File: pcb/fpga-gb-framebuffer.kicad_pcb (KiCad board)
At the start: 2 copper layers, 74.9 x 45.7 mm, 20 parts

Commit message: Updated PCB design
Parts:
- moved GB_LCD1 3.81 mm to (100.3, 69.8)
- moved R1 3.81 mm to (108.0, 72.4)
- moved R2 3.81 mm to (115.6, 69.8)
- moved R3 3.81 mm to (108.0, 77.5)
- moved R4 3.81 mm to (115.6, 74.9)
- moved R6 2.54 mm to (115.6, 82.6)
- moved R7 2.54 mm to (108.0, 92.7)
- moved R5 2.54 mm to (108.0, 85.1)
- moved R8 2.54 mm to (115.6, 90.2)
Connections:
- TinyFPGA_BX1 pad 10: IN_DATA_1 -> Net-(TinyFPGA_BX1-Pad10)
- TinyFPGA_BX1 pad 11: Net-(TinyFPGA_BX1-Pad11) -> IN_PIXEL_CLK
- TinyFPGA_BX1 pad 12: IN_PIXEL_CLK -> Net-(TinyFPGA_BX1-Pad12)
- TinyFPGA_BX1 pad 6: Net-(TinyFPGA_BX1-Pad6) -> IN_DATA_0
- TinyFPGA_BX1 pad 8: Net-(TinyFPGA_BX1-Pad8) -> IN_DATA_1
- TinyFPGA_BX1 pad 9: IN_DATA_0 -> Net-(TinyFPGA_BX1-Pad9)
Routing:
- net GB_GND: track 153.8 -> 0.00 mm
- net GB_PIXEL_CLK: track 10.8 -> 13.3 mm
- net GB_VSYNC: track 11.3 -> 13.3 mm
- net IN_DATA_0: track 8.01 -> 6.44 mm
- net IN_DATA_1: track 6.96 -> 6.44 mm

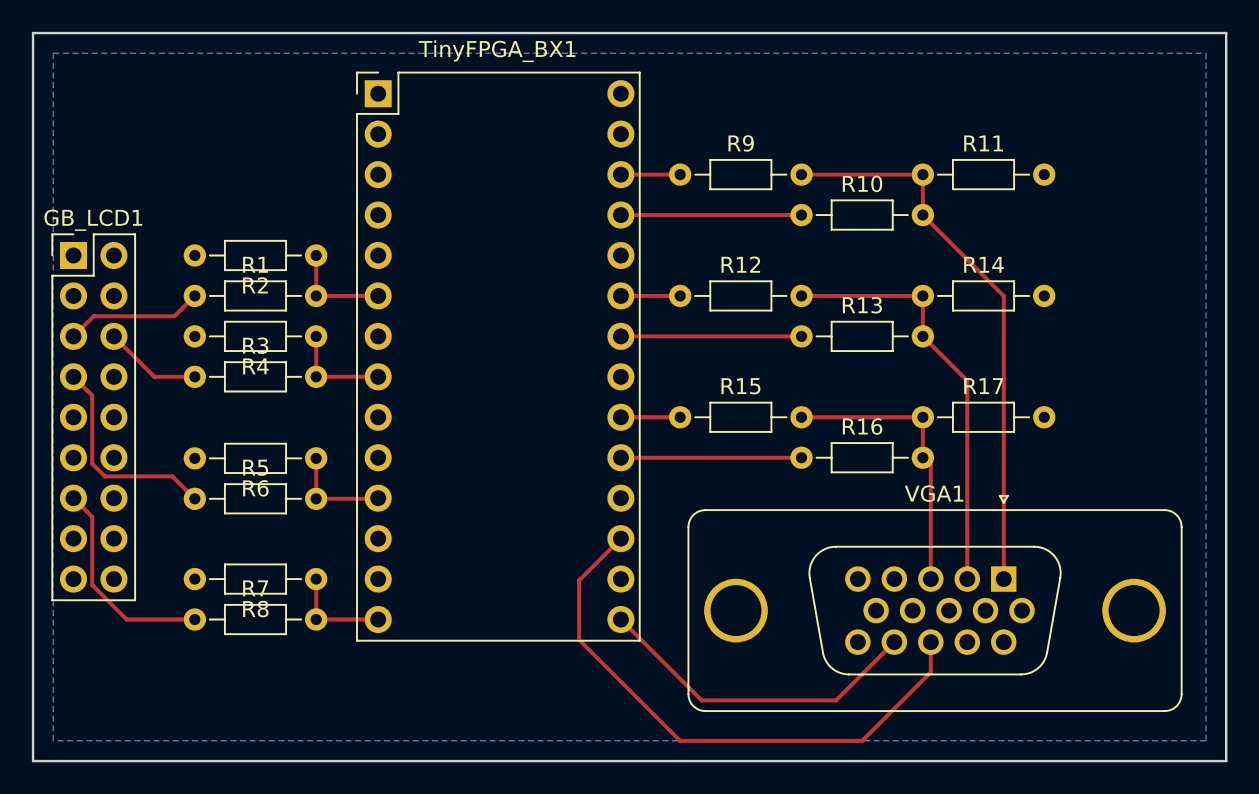
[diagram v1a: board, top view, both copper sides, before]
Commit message: Schematic update with tinyfpga symbol and pin assignment update for VGA
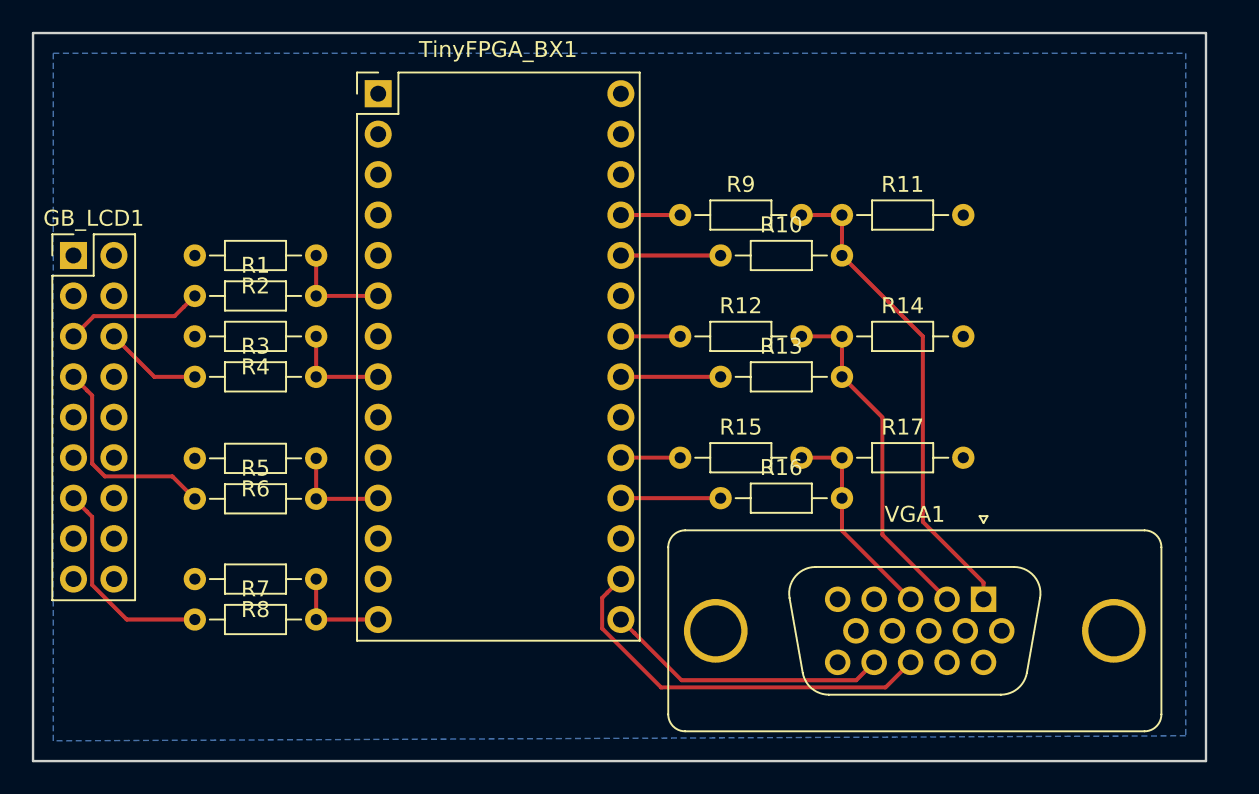
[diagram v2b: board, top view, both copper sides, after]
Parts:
- TinyFPGA_BX1: value Conn_02x14_Odd_Even -> FPGA
- moved R16 5.68 mm to (141.0, 85.1)
- moved R10 5.68 mm to (141.0, 69.8)
- moved R13 5.68 mm to (141.0, 77.5)
- moved R11 5.68 mm to (148.6, 67.3)
- moved R14 5.68 mm to (148.6, 74.9)
- moved R17 5.68 mm to (148.6, 82.5)
- moved R12 2.54 mm to (138.4, 74.9)
- moved R9 2.54 mm to (138.4, 67.3)
- moved R15 2.54 mm to (138.4, 82.5)
- moved VGA1 1.80 mm to (157.5, 91.4)
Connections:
- TinyFPGA_BX1 pad 16: Net-(TinyFPGA_BX1-Pad16) -> VGA_HSYNC
- TinyFPGA_BX1 pad 17: VGA_HSYNC -> Net-(TinyFPGA_BX1-Pad17)
- TinyFPGA_BX1 pad 18: Net-(TinyFPGA_BX1-Pad18) -> OUT_B_1
- TinyFPGA_BX1 pad 19: OUT_B_1 -> OUT_B_0
- TinyFPGA_BX1 pad 20: OUT_B_0 -> Net-(TinyFPGA_BX1-Pad20)
- TinyFPGA_BX1 pad 21: Net-(TinyFPGA_BX1-Pad21) -> OUT_G_1
- TinyFPGA_BX1 pad 22: OUT_G_1 -> OUT_G_0
- TinyFPGA_BX1 pad 23: OUT_G_0 -> Net-(TinyFPGA_BX1-Pad23)
- TinyFPGA_BX1 pad 24: Net-(TinyFPGA_BX1-Pad24) -> OUT_R_1
- TinyFPGA_BX1 pad 25: OUT_R_1 -> OUT_R_0
- TinyFPGA_BX1 pad 26: OUT_R_0 -> Net-(TinyFPGA_BX1-Pad26)
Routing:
- net VGA_HSYNC: track 35.8 -> 25.1 mm
- net OUT_R_1: track 11.3 -> 6.26 mm
- net OUT_G_1: track 11.3 -> 6.26 mm
- net OUT_B_1: track 11.3 -> 6.26 mm
- net VGA_R: track 35.1 -> 30.4 mm
- net VGA_G: track 26.6 -> 21.8 mm
- net VGA_B: track 18.0 -> 13.2 mm
- net VGA_VSYNC: track 20.8 -> 18.0 mm
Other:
- board size 74.9 x 45.7 mm -> 73.7 x 45.7 mm
